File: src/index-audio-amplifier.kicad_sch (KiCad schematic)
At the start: 60 parts, among them J1 CU3616SASCLA004-LF, J2 SWD_PicoprobeCandybar, J3 Conn_01x02, J4 Conn_01x02, U1 RP2040, U2 RT6150B-33GQW, U3 W25Q16JVUXIQ, U4 MAX98360CENL, U5 TLV70033_SOT23-5, U6 MAX98360CENL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

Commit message: Add & associate dual stack USB-C port footprint
Uses placeholder Frankenstein model
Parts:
- J1: footprint (none) -> ProjectFootprints_IndexAudioAmplifier:USB_C_Receptacle_CviLux_CU36SASCLA004-LF
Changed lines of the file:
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@@
 			)
 		)
-		(property "Footprint" ""
+		(property "Footprint" "ProjectFootprints_IndexAudioAmplifier:USB_C_Receptacle_CviLux_CU36SASCLA004-LF"
 			(at 200.66 40.64 0)
 			(effects
@@
 	)
 	(symbol
-		(lib_name "CU3616SASCLA004-LF_1")
 		(lib_id "ProjectSymbols_IndexAudioAmplifier:CU3616SASCLA004-LF")
 		(at 29.21 40.64 0)
@@
 			)
 		)
-		(property "Footprint" ""
+		(property "Footprint" "ProjectFootprints_IndexAudioAmplifier:USB_C_Receptacle_CviLux_CU36SASCLA004-LF"
 			(at 29.21 40.64 0)
 			(effects

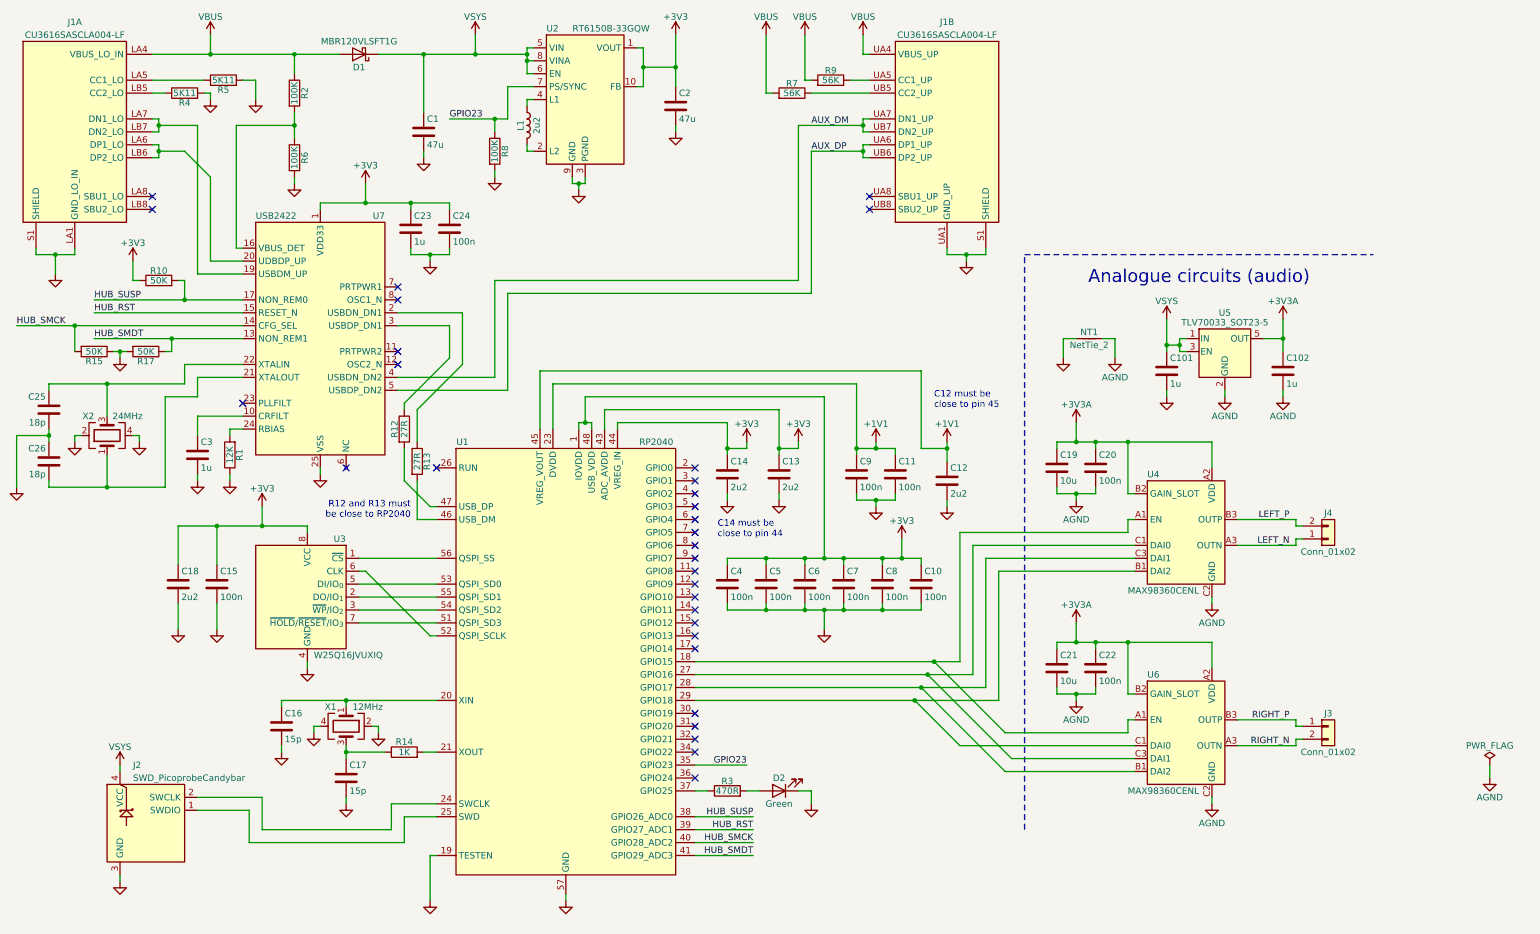
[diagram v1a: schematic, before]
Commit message: Add back mounting hole & more net labels
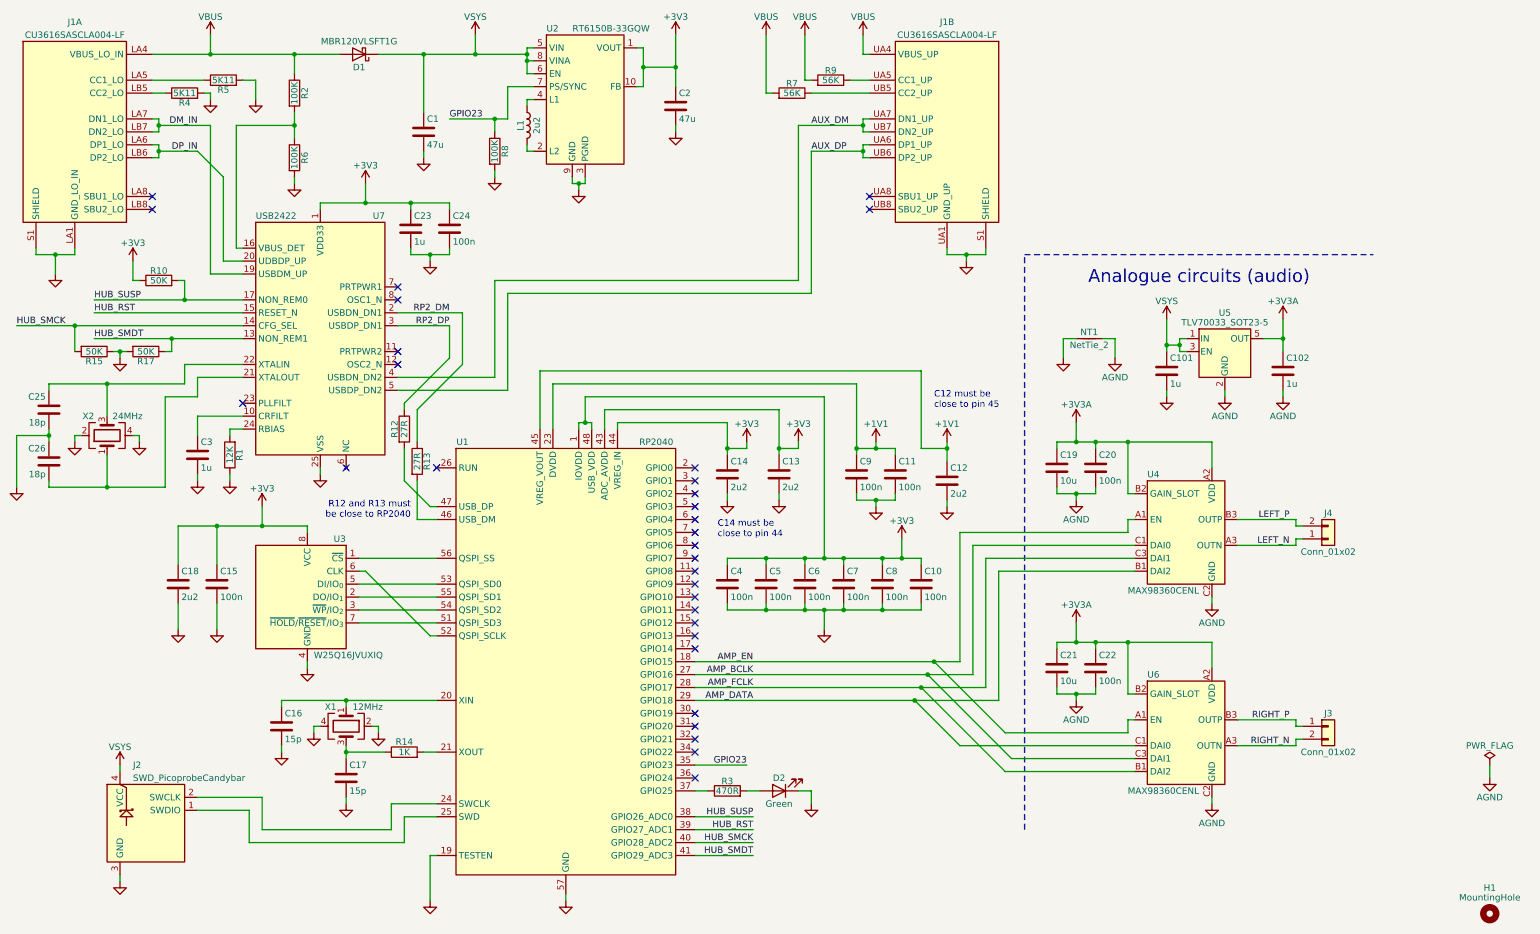
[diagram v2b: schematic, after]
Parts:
- added H1: MountingHole, MountingHole:MountingHole_2.2mm_M2_ISO7380, symbol Mechanical:MountingHole
- X2: footprint (none) -> Crystal:Crystal_SMD_3225-4Pin_3.2x2.5mm
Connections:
- net RP2_DP: now reaches R12.1, U7.3 (USBDP_DN1)
- net DM_IN: now reaches J1.LA7 (DN1_LO), J1.LB7 (DN2_LO), U7.19 (USBDM_UP)
- net RP2_DM: now reaches R13.1, U7.2 (USBDN_DN1)
- net DP_IN: now reaches J1.LA6 (DP1_LO), J1.LB6 (DP2_LO), U7.20 (UDBDP_UP)
- net AMP_EN: now reaches U1.18 (GPIO15), U4.A1 (EN), U6.A1 (EN)
- net AMP_DATA: now reaches U1.29 (GPIO18), U4.B1 (DAI2), U6.C1 (DAI0)
- net AMP_BCLK: now reaches U1.27 (GPIO16), U4.C1 (DAI0), U6.C3 (DAI1)
- net AMP_FCLK: now reaches U1.28 (GPIO17), U4.C3 (DAI1), U6.B1 (DAI2)
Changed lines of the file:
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@@
 	(wire
 		(pts
-			(xy 53.34 39.37) (xy 53.34 68.58)
+			(xy 55.88 39.37) (xy 55.88 68.58)
 		)
 		(stroke
@@
 	(wire
 		(pts
-			(xy 55.88 49.53) (xy 55.88 66.04)
+			(xy 58.42 49.53) (xy 58.42 66.04)
 		)
 		(stroke
@@
 	(wire
 		(pts
+			(xy 45.72 44.45) (xy 53.34 44.45)
+		)
+		(stroke
+			(width 0)
+			(type default)
+		)
+	)
+	(wire
+		(pts
 			(xy 35.56 104.14) (xy 35.56 110.49)
 		)
@@
 	(wire
 		(pts
-			(xy 45.72 44.45) (xy 50.8 44.45)
-		)
-		(stroke
-			(width 0)
-			(type default)
-		)
-	)
-	(wire
-		(pts
 			(xy 257.81 156.21) (xy 269.24 156.21)
 		)
@@
 	(wire
 		(pts
-			(xy 50.8 44.45) (xy 55.88 49.53)
+			(xy 53.34 44.45) (xy 58.42 49.53)
 		)
 		(stroke
@@
 	(wire
 		(pts
-			(xy 55.88 66.04) (xy 62.23 66.04)
+			(xy 58.42 66.04) (xy 62.23 66.04)
 		)
 		(stroke
@@
 	(wire
 		(pts
-			(xy 53.34 68.58) (xy 62.23 68.58)
+			(xy 55.88 68.58) (xy 62.23 68.58)
 		)
 		(stroke
@@
 	(wire
 		(pts
+			(xy 45.72 39.37) (xy 55.88 39.37)
+		)
+		(stroke
+			(width 0)
+			(type default)
+		)
+	)
+	(wire
+		(pts
 			(xy 157.48 102.87) (xy 157.48 104.14)
 		)
@@
 		)
 	)
-	(wire
-		(pts
-			(xy 53.34 39.37) (xy 45.72 39.37)
-		)
-		(stroke
-			(width 0)
-			(type default)
-		)
-	)
 	(label "HUB_SUSP"
 		(at 162.56 175.26 180)
@@
 		)
 	)
+	(label "AMP_FCLK"
+		(at 162.56 149.86 180)
+		(effects
+			(font
+				(size 1.27 1.27)
+			)
+			(justify right bottom)
+		)
+	)
 	(label "RIGHT_N"
 		(at 267.97 161.29 180)
@@
 		)
 	)
+	(label "AMP_DATA"
+		(at 162.56 152.4 180)
+		(effects
+			(font
+				(size 1.27 1.27)
+			)
+			(justify right bottom)
+		)
+	)
 	(label "HUB_SUSP"
 		(at 33.02 73.66 0)
@@
 		)
 	)
+	(label "AMP_EN"
+		(at 162.56 144.78 180)
+		(effects
+			(font
+				(size 1.27 1.27)
+			)
+			(justify right bottom)
+		)
+	)
+	(label "AMP_BCLK"
+		(at 162.56 147.32 180)
+		(effects
+			(font
+				(size 1.27 1.27)
+			)
+			(justify right bottom)
+		)
+	)
 	(label "GPIO23"
 		(at 102.87 38.1 0)
@@
 		)
 	)
+	(label "DP_IN"
+		(at 53.34 44.45 180)
+		(effects
+			(font
+				(size 1.27 1.27)
+			)
+			(justify right bottom)
+		)
+	)
 	(label "GPIO23"
 		(at 161.29 165.1 180)
@@
 		)
 	)
+	(label "RP2_DP"
+		(at 102.87 78.74 180)
+		(effects
+			(font
+				(size 1.27 1.27)
+			)
+			(justify right bottom)
+		)
+	)
 	(label "RIGHT_P"
 		(at 267.97 156.21 180)
@@
 		)
 	)
+	(label "DM_IN"
+		(at 53.34 39.37 180)
+		(effects
+			(font
+				(size 1.27 1.27)
+			)
+			(justify right bottom)
+		)
+	)
 	(label "LEFT_N"
 		(at 267.97 121.92 180)
@@
 		)
 	)
+	(label "RP2_DM"
+		(at 102.87 76.2 180)
+		(effects
+			(font
+				(size 1.27 1.27)
+			)
+			(justify right bottom)
+		)
+	)
 	(symbol
 		(lib_id "power:GND")
@@
 			)
 		)
-		(property "Footprint" ""
+		(property "Footprint" "Crystal:Crystal_SMD_3225-4Pin_3.2x2.5mm"
 			(at 35.56 100.33 0)
 			(effects
@@
 					(unit 1)
 				)
+			)
+		)
+	)
+	(symbol
+		(lib_id "Mechanical:MountingHole")
+		(at 307.34 194.31 0)
+		(unit 1)
+		(exclude_from_sim no)
+		(in_bom no)
+		(on_board yes)
+		(dnp no)
+		(property "Reference" "H1"
+			(at 307.34 189.23 0)
+			(effects
+				(font
+					(size 1.27 1.27)
+				)
+			)
+		)
+		(property "Value" "MountingHole"
+			(at 307.34 191.135 0)
+			(effects
+				(font
+					(size 1.27 1.27)
+				)
+			)
+		)
+		(property "Footprint" "MountingHole:MountingHole_2.2mm_M2_ISO7380"
+			(at 307.34 194.31 0)
+			(effects
+				(font
+					(size 1.27 1.27)
+				)
+				(hide yes)
+			)
+		)
+		(property "Datasheet" "~"
+			(at 307.34 194.31 0)
+			(effects
+				(font
+					(size 1.27 1.27)
+				)
+				(hide yes)
+			)
+		)
+		(property "Description" "Mounting Hole without connection"
+			(at 307.34 194.31 0)
+			(effects
+				(font
+					(size 1.27 1.27)
+				)
+				(hide yes)
+			)
+		)
+		(instances
+			(project ""
+				(path "/dc35f43b-99fc-498e-a143-7e0669c7658b"
+					(reference "H1")
+					(unit 1)
+				)

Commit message: Update USB2422 footprint to use thermal vias
Per VSS pin description in datasheet:
<https://ww1.microchip.com/downloads/aemDocuments/documents/OTH/ProductDocuments/DataSheets/00001726B.pdf#G4.1051294>
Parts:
- U7: footprint Package_DFN_QFN:VQFN-24-1EP_4x4mm_P0.5mm_EP2.5x2.5mm -> Package_DFN_QFN:VQFN-24-1EP_4x4mm_P0.5mm_EP2.5x2.5mm_ThermalVias
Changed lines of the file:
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@@
 			)
 		)
-		(property "Footprint" "Package_DFN_QFN:VQFN-24-1EP_4x4mm_P0.5mm_EP2.5x2.5mm"
+		(property "Footprint" "Package_DFN_QFN:VQFN-24-1EP_4x4mm_P0.5mm_EP2.5x2.5mm_ThermalVias"
 			(at 77.47 120.65 0)
 			(effects

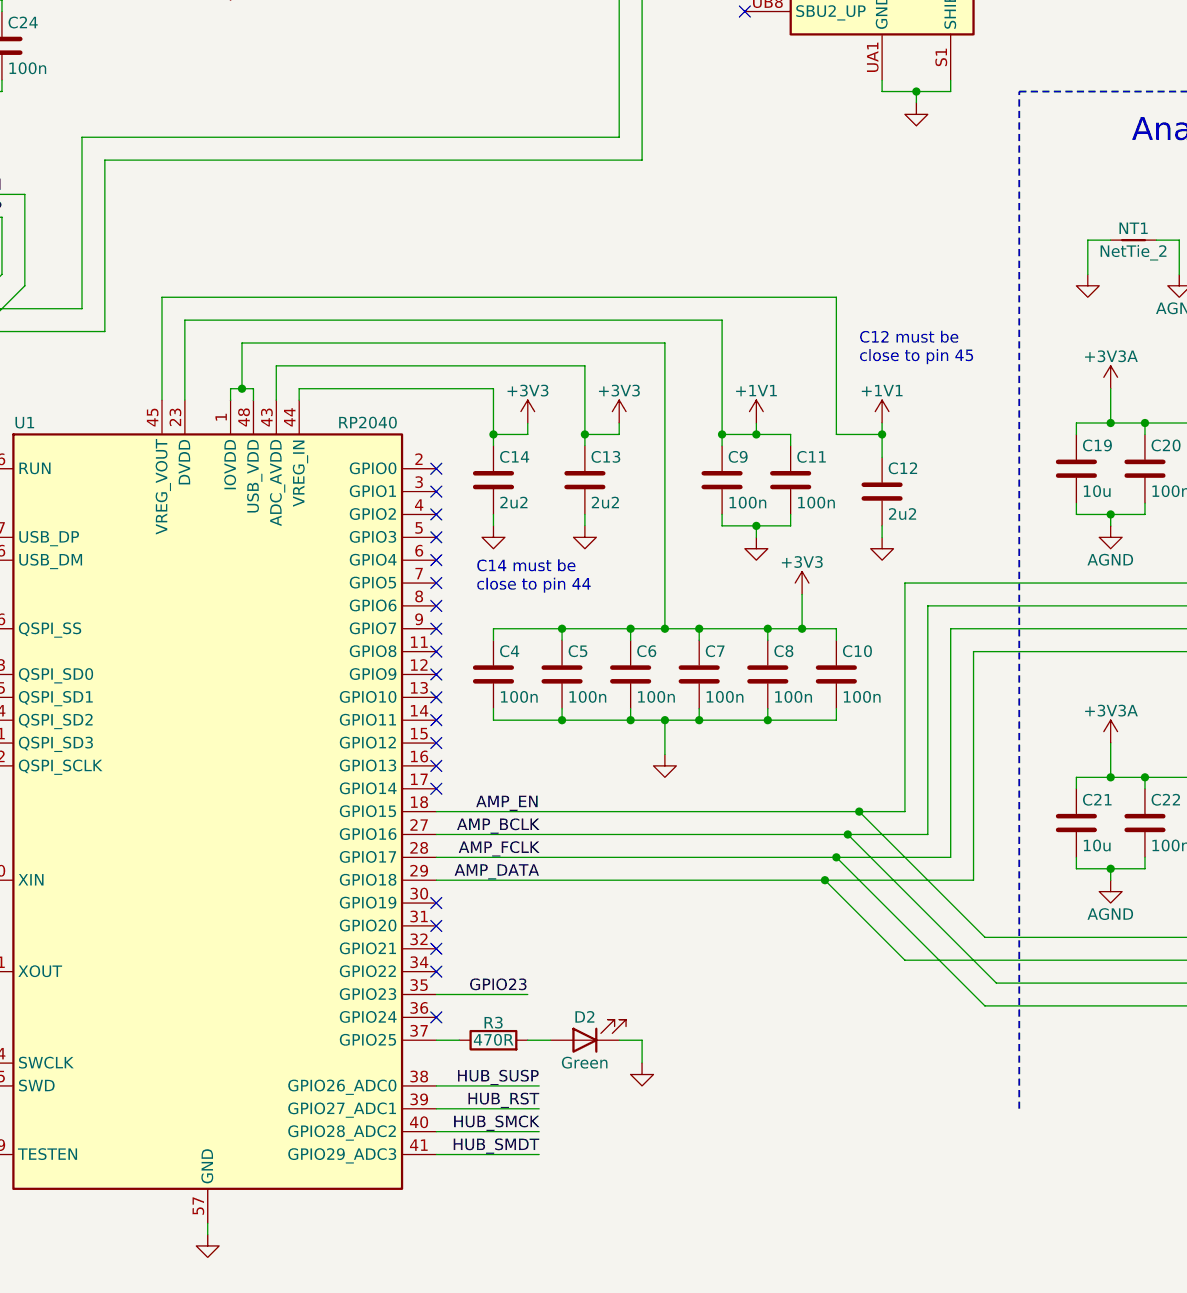
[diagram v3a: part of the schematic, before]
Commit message: Move USB2422 controls to GPIO0-3 to assist layout
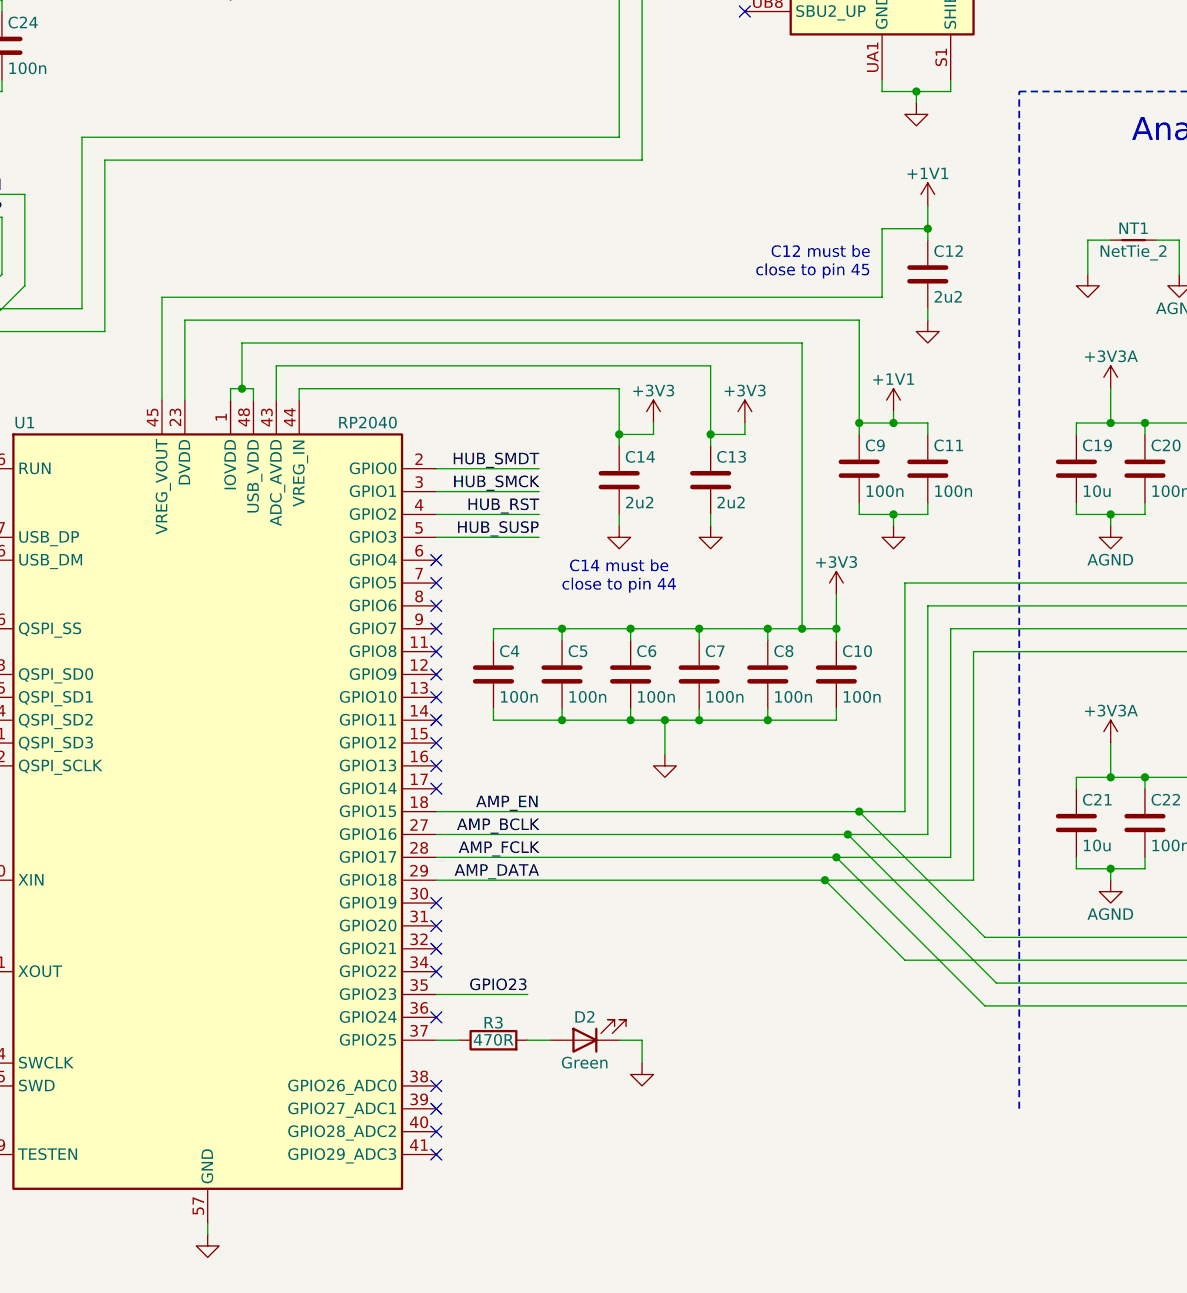
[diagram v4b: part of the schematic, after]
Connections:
- net HUB_RST: now also U1.4 (GPIO2); no longer U1.39 (GPIO27_ADC1)
- net HUB_SMCK: now also U1.3 (GPIO1); no longer U1.40 (GPIO28_ADC2)
- net HUB_SMDT: now also U1.2 (GPIO0); no longer U1.41 (GPIO29_ADC3)
- net HUB_SUSP: now also U1.5 (GPIO3); no longer U1.38 (GPIO26_ADC0)
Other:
- moved on the sheet: C11, C12, C13, C14, C9

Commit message: Continue refactoring very compact layout
Feeling pretty good about this second attempt so far...
Next up: analogue and power regulation
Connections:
- net LED: now reaches R3.1, U1.37 (GPIO25)
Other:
- moved on the sheet: D2, R3
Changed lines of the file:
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@@
 	(wire
 		(pts
-			(xy 173.99 172.72) (xy 173.99 170.18)
+			(xy 182.88 172.72) (xy 182.88 170.18)
 		)
 		(stroke
@@
 	(wire
 		(pts
-			(xy 161.29 170.18) (xy 163.83 170.18)
+			(xy 170.18 170.18) (xy 172.72 170.18)
 		)
 		(stroke
@@
 	(wire
 		(pts
-			(xy 151.13 170.18) (xy 153.67 170.18)
+			(xy 151.13 170.18) (xy 162.56 170.18)
 		)
 		(stroke
@@
 	(wire
 		(pts
-			(xy 173.99 170.18) (xy 171.45 170.18)
+			(xy 182.88 170.18) (xy 180.34 170.18)
 		)
 		(stroke
@@
 		)
 	)
+	(label "LED"
+		(at 161.29 170.18 180)
+		(effects
+			(font
+				(size 1.27 1.27)
+			)
+			(justify right bottom)
+		)
+	)
 	(label "LEFT_N"
 		(at 267.97 121.92 180)
@@
 	(symbol
 		(lib_id "Device:LED")
-		(at 167.64 170.18 180)
+		(at 176.53 170.18 180)
 		(unit 1)
 		(exclude_from_sim no)
@@
 		(dnp no)
 		(property "Reference" "D2"
-			(at 167.64 167.64 0)
+			(at 176.53 167.64 0)
 			(effects
 				(font
@@
 		)
 		(property "Value" "Green"
-			(at 167.64 172.72 0)
+			(at 176.53 172.72 0)
 			(effects
 				(font
@@
 		)
 		(property "Footprint" "LED_SMD:LED_0603_1608Metric"
-			(at 167.64 170.18 0)
+			(at 176.53 170.18 0)
 			(effects
 				(font
@@
 		)
 		(property "Datasheet" "~"
-			(at 167.64 170.18 0)
+			(at 176.53 170.18 0)
 			(effects
 				(font
@@
 		)
 		(property "Description" "Light emitting diode"
-			(at 167.64 170.18 0)
+			(at 176.53 170.18 0)
 			(effects
 				(font
@@
 		)
 		(property "Sim.Pins" "1=K 2=A"
-			(at 167.64 170.18 0)
+			(at 176.53 170.18 0)
 			(effects
 				(font
@@
 	(symbol
 		(lib_id "Device:R")
-		(at 157.48 170.18 90)
+		(at 166.37 170.18 90)
 		(unit 1)
 		(exclude_from_sim no)
@@
 		(dnp no)
 		(property "Reference" "R3"
-			(at 157.48 168.275 90)
+			(at 166.37 168.275 90)
 			(effects
 				(font
@@
 		)
 		(property "Value" "470R"
-			(at 157.48 170.18 90)
+			(at 166.37 170.18 90)
 			(effects
 				(font
@@
 		)
 		(property "Footprint" "Resistor_SMD:R_0402_1005Metric"
-			(at 157.48 171.958 90)
+			(at 166.37 171.958 90)
 			(effects
 				(font
@@
 		)
 		(property "Datasheet" "~"
-			(at 157.48 170.18 0)
+			(at 166.37 170.18 0)
 			(effects
 				(font
@@
 		)
 		(property "Description" "Resistor"
-			(at 157.48 170.18 0)
+			(at 166.37 170.18 0)
 			(effects
 				(font
@@
 	(symbol
 		(lib_id "power:GND")
-		(at 173.99 172.72 0)
+		(at 182.88 172.72 0)
 		(unit 1)
 		(exclude_from_sim no)
@@
 		(dnp no)
 		(property "Reference" "#PWR021"
-			(at 173.99 179.07 0)
+			(at 182.88 179.07 0)
 			(effects
 				(font
@@
 		)
 		(property "Value" "GND"
-			(at 173.99 176.53 0)
+			(at 182.88 176.53 0)
 			(effects
 				(font
@@
 		)
 		(property "Footprint" ""
-			(at 173.99 172.72 0)
+			(at 182.88 172.72 0)
 			(effects
 				(font
@@
 		)
 		(property "Datasheet" ""
-			(at 173.99 172.72 0)
+			(at 182.88 172.72 0)
 			(effects
 				(font
@@
 		)
 		(property "Description" "Power symbol creates a global label with name \"GND\" , ground"
-			(at 173.99 172.72 0)
+			(at 182.88 172.72 0)
 			(effects
 				(font
